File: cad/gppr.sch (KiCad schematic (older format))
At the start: 13 parts

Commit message: create complete schematic
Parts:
- removed C?: C, symbol Device:C
- removed TP?: TestPoint_2Pole, symbol Connector:TestPoint_2Pole
- removed U?: TPS7A470X, Package_DFN_QFN:QFN-20-1EP_5x5mm_P0.65mm_EP3.35x3.35mm, symbol texas_instruments:TPS7A470X
- added C1, C2, C4: 10uF, Capacitor_SMD:C_0805_2012Metric, symbol Device:C
- added C10, C3, C5: 1uF, Capacitor_SMD:C_0805_2012Metric, symbol Device:C
- added C6, C7, C8: 1000uF, Capacitor_SMD:CP_Elec_16x17.5, symbol Device:CP
- added D2, D3, D4: MURS120, Diode_SMD:D_SMB, symbol Device:D
- added H2, H3, H4: MountingHole, MountingHole:MountingHole_3.2mm_M3_DIN965, symbol Mechanical:MountingHole
- added R10: 1KΩ, Resistor_SMD:R_0805_2012Metric, symbol Device:R
- added R2, R3, R4, R5, R6, R7, R8, R9: 0Ω, Resistor_SMD:R_0805_2012Metric_Pad1.15x1.40mm_HandSolder, symbol Device:R
- added TP1, TP2, TP3: TestPoint_2Pole, Connector_pin_header:PinHeader_1x02_P2.54mm_Vertical, symbol Connector:TestPoint_2Pole
- added U1: TPS7A470X, Housings_DFN_QFN:Texas_VQFN-RGW-20, symbol texas_instruments:TPS7A470X
- C9: renamed from C?; value CP -> 1000uF; footprint (none) -> Capacitor_SMD:CP_Elec_16x17.5
- D1: renamed from D?; value D -> MURS120; footprint (none) -> Diode_SMD:D_SMB
- D5: renamed from D?; value D_Zener -> 1SMB5927BT3G; footprint (none) -> Diode_SMD:D_SMB
- D6: renamed from D?; value LED -> LED_POWER; footprint (none) -> LED_SMD:LED_0805_2012Metric
- H1: renamed from H?; footprint (none) -> MountingHole:MountingHole_3.2mm_M3_DIN965
- J3: renamed from J?; footprint (none) -> Connector_Coaxial:U.FL_Molex_MCRF_73412-0110_Vertical
- Q1: renamed from Q?; value QM6006D -> IRLR2908
- R1: renamed from R?; value R -> 13KΩ; footprint (none) -> Resistor_SMD:R_0805_2012Metric
- gave numbers to parts that had none: 2
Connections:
- net at Q1.1 (G): now also D5.1 (K), R1.1, C1.1
- net at Q1.2 (D): now also C9.1, D1.1 (K), R1.2, C6.1, C7.1, C8.1, D3.1 (K), TP1.1
- net at Q1.3 (S): now also D5.2 (A), C2.1, C3.1, TP2.1, U1.13 (EN), U1.15 (IN), U1.16 (IN)
- net at D1.2 (A): now also J1.2 (Pin_2), J1.4 (Pin_4), D2.1 (K)
- net GND: now reaches C9.2
- net GND: now also D6.1 (K), J2.2 (Pin_2), J3.2 (Ext), C1.2, C10.2, C2.2, C3.2, C4.2, C5.2, C6.2, C7.2, C8.2, D2.2 (A), D4.2 (A), R2.2, R3.2, R4.2, R5.2, R6.2, R7.2, R8.2, R9.2, TP1.2, TP2.2, TP3.2, U1.21 (PAD), U1.7 (GND)
- net at D6.2 (A): now also R10.1
- net at J1.1 (Pin_1): now also J1.3 (Pin_3), D3.2 (A), D4.1 (K)
- net at J2.1 (Pin_1): now also J3.1 (In), C4.1, C5.1, R10.2, TP3.1, U1.1 (OUT), U1.20 (OUT), U1.3 (SENSE/FB)
- new net: R4.1, U1.10 (0P4V)
- new net: R3.1, U1.11 (0P2V)
- new net: R2.1, U1.12 (0P1V)
- new net: C10.1, U1.14 (NR)
- new net: R9.1, U1.4 (6P4V2)
- new net: R8.1, U1.5 (6P4V1)
- new net: R7.1, U1.6 (3P2V)
- new net: R6.1, U1.8 (1P6V)
- new net: R5.1, U1.9 (0P8V)
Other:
- moved on the sheet: C9, D1, D5, D6, H1, J1, J2, J3, Q1, R1

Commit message: update schematic: remove any-out, use resistor-divider fb on regulator instead
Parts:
- removed R4, R5, R6, R7, R8, R9: 0Ω, Resistor_SMD:R_0805_2012Metric_Pad1.15x1.40mm_HandSolder, symbol Device:R
- R1: renamed from R2; value 0Ω -> 76.8KΩ
- R2: renamed from R3; value 0Ω -> 10.2KΩ
- renumbered R10 to R3, R1 to R4
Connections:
- net GND: now also R2.1; no longer R1.2, R2.2
- net at C4.1, C5.1, J2.1 (Pin_1)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: now also R1.2; no longer U1.3 (SENSE/FB)
- net at U1.11 (0P2V): no longer R2.1
- net at U1.12 (0P1V): no longer R1.1
- new net: R1.1, R2.2, U1.3 (SENSE/FB)
- no-connect marks 0 -> 8
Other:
- moved on the sheet: C4, C5, R1, R2

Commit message: add missing footprint references for in/out connectors
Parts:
- J1: footprint (none) -> Connector_Molex:Molex_Mini-Fit_Jr_5566-04A_2x02_P4.20mm_Vertical
- J2: footprint (none) -> Connector_Molex:Molex_Mini-Fit_Jr_5566-02A_2x01_P4.20mm_Vertical
- Q1: footprint Package_TO_SOT_SMD:TO-252-2 -> TO_SOT_Packages_SMD:TO-252-2
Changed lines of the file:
@@
 F 0 "Q1" H 4805 4146 50  0000 L CNN
 F 1 "IRLR2908" H 4805 4055 50  0000 L CNN
-F 2 "Package_TO_SOT_SMD:TO-252-2" H 4800 4025 50  0001 L CIN
+F 2 "TO_SOT_Packages_SMD:TO-252-2" H 4800 4025 50  0001 L CIN
 F 3 "https://www.infineon.com/dgdl/irlr2908pbf.pdf?fileId=5546d462533600a40153566cdace2681" H 4400 4400 50  0001 L CNN
 	1    4600 4100
@@
 F 0 "J1" H 600 5000 50  0000 L CNN
 F 1 "Conn_01x04_Female" H -50 5100 50  0000 L CNN
-F 2 "" H 750 4500 50  0001 C CNN
+F 2 "Connector_Molex:Molex_Mini-Fit_Jr_5566-04A_2x02_P4.20mm_Vertical" H 750 4500 50  0001 C CNN
 F 3 "~" H 750 4500 50  0001 C CNN
 	1    750  4500
@@
 F 0 "J2" H 10650 4300 50  0000 L CNN
 F 1 "Conn_01x02_Female" H 10150 4200 50  0000 L CNN
-F 2 "" H 10900 4000 50  0001 C CNN
+F 2 "Connector_Molex:Molex_Mini-Fit_Jr_5566-02A_2x01_P4.20mm_Vertical" H 10900 4000 50  0001 C CNN
 F 3 "~" H 10900 4000 50  0001 C CNN
 	1    10900 4000

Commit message: add simple calcs for max input voltage for safe operation
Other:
- note added: "Capacitors: Panasonic EEV-FK1H102M"
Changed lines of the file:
@@
 	7050 4550 7050 4000
 Connection ~ 7050 4000
+Text Notes 2300 3850 0    50   ~ 0
+Capacitors: Panasonic EEV-FK1H102M
 $EndSCHEMATC

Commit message: generate netlist
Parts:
- J1: footprint Connector_Molex:Molex_Mini-Fit_Jr_5566-04A_2x02_P4.20mm_Vertical -> Connector_Molex:Molex_Micro-Fit_3.0_43045-0412_2x02_P3.00mm_Vertical
- J2: footprint Connector_Molex:Molex_Mini-Fit_Jr_5566-02A_2x01_P4.20mm_Vertical -> Connector_Molex:Molex_Micro-Fit_3.0_43045-0212_2x01_P3.00mm_Vertical
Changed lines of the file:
@@
 F 0 "J1" H 600 5000 50  0000 L CNN
 F 1 "Conn_01x04_Female" H -50 5100 50  0000 L CNN
-F 2 "Connector_Molex:Molex_Mini-Fit_Jr_5566-04A_2x02_P4.20mm_Vertical" H 750 4500 50  0001 C CNN
+F 2 "Connector_Molex:Molex_Micro-Fit_3.0_43045-0412_2x02_P3.00mm_Vertical" H 750 4500 50  0001 C CNN
 F 3 "~" H 750 4500 50  0001 C CNN
 	1    750  4500
@@
 F 0 "J2" H 10650 4300 50  0000 L CNN
 F 1 "Conn_01x02_Female" H 10150 4200 50  0000 L CNN
-F 2 "Connector_Molex:Molex_Mini-Fit_Jr_5566-02A_2x01_P4.20mm_Vertical" H 10900 4000 50  0001 C CNN
+F 2 "Connector_Molex:Molex_Micro-Fit_3.0_43045-0212_2x01_P3.00mm_Vertical" H 10900 4000 50  0001 C CNN
 F 3 "~" H 10900 4000 50  0001 C CNN
 	1    10900 4000

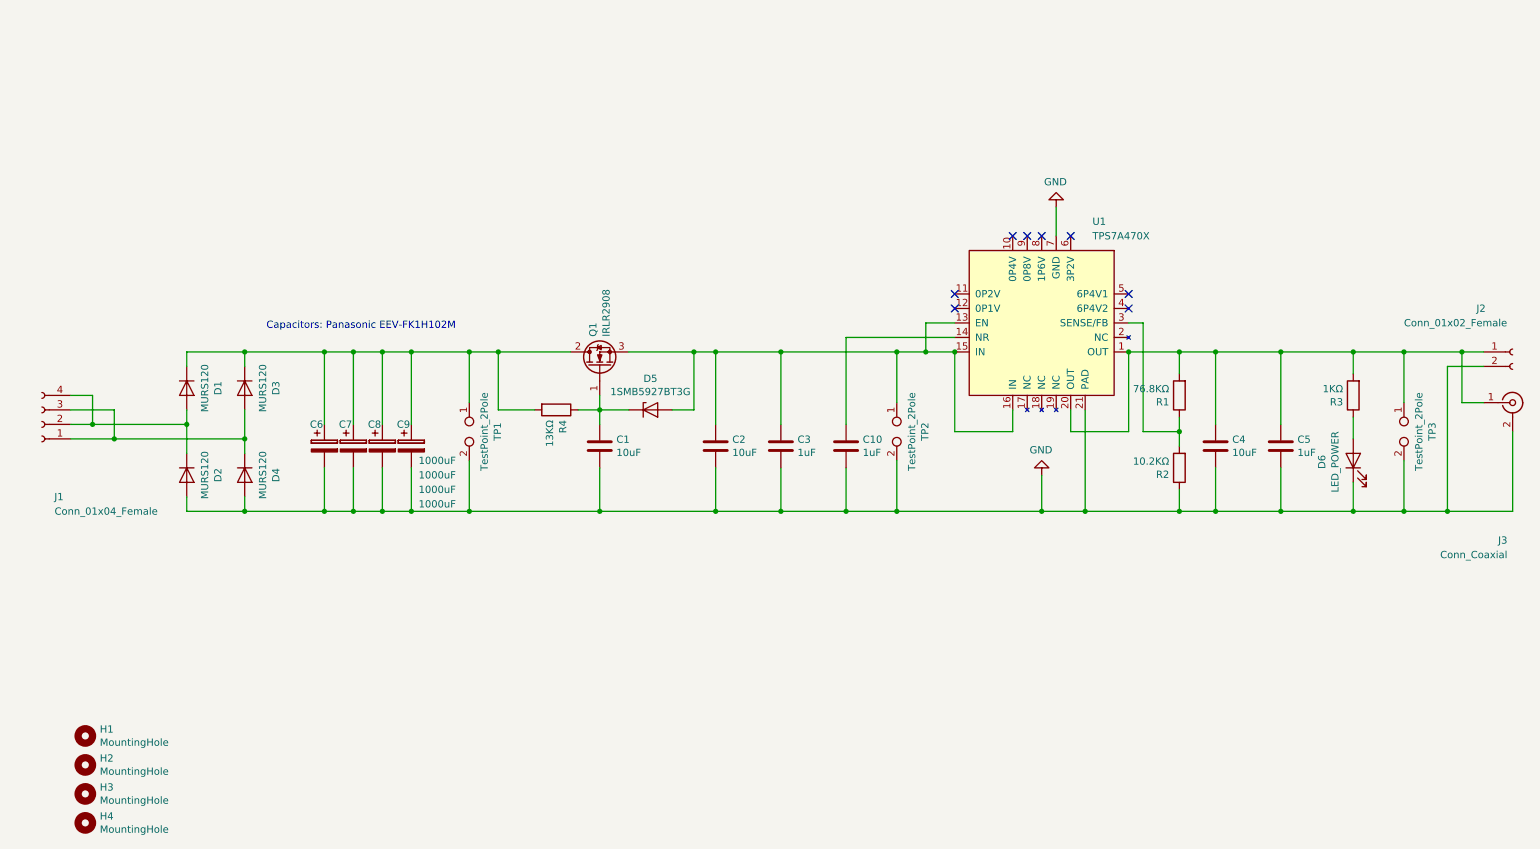
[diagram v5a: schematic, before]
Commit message: add jumper-resistors, change ceramic film capacitor packages
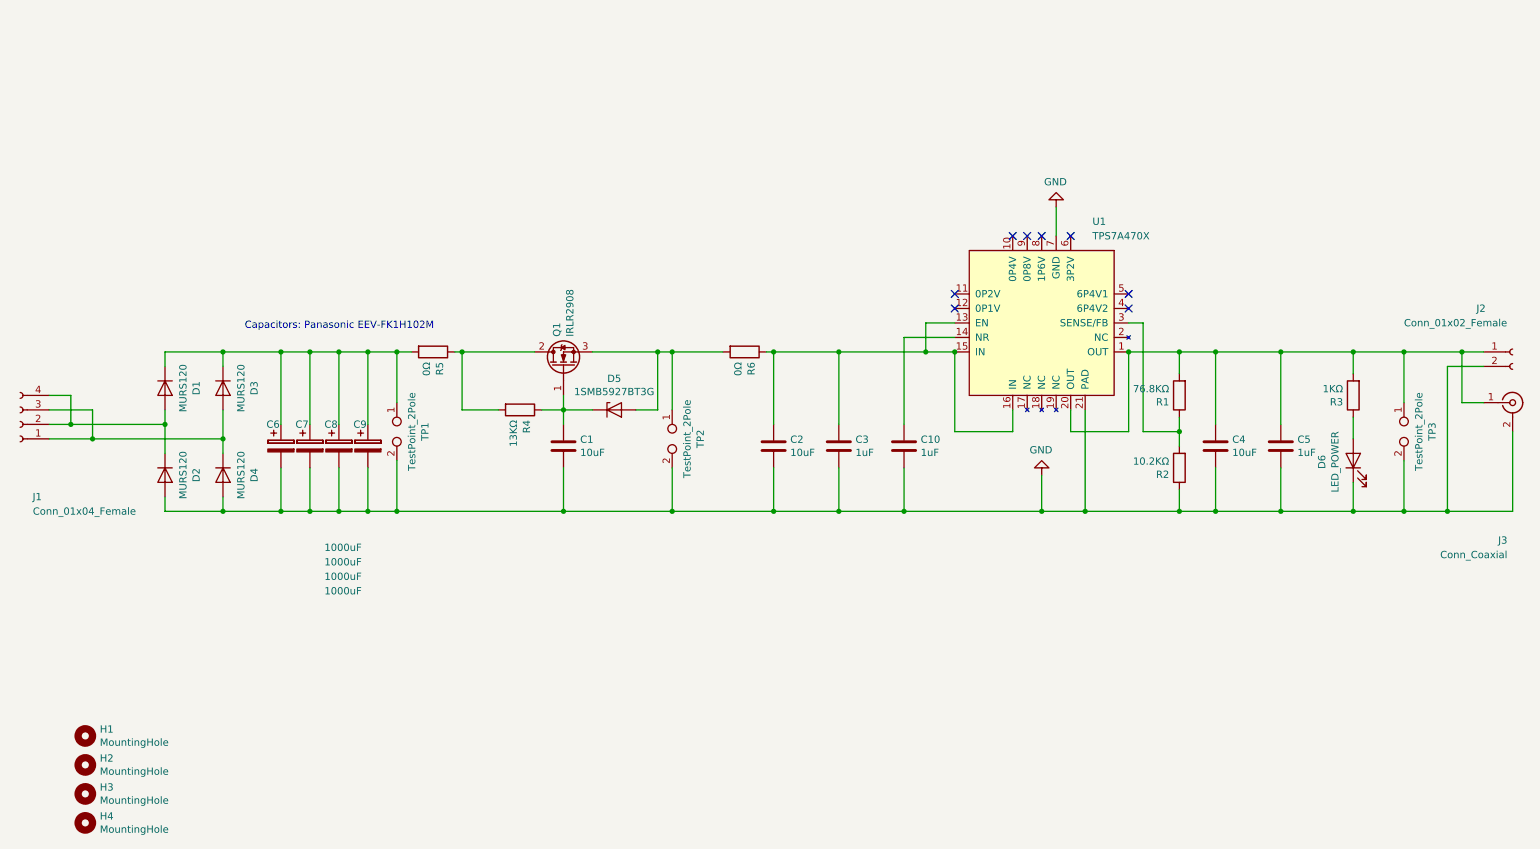
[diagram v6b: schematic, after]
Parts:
- added R5, R6: 0Ω, Resistor_SMD:R_0805_2012Metric, symbol Device:R
- C1, C2, C4: footprint Capacitor_SMD:C_0805_2012Metric -> Capacitor_SMD:C_1210_3225Metric
- C10, C3, C5: footprint Capacitor_SMD:C_0805_2012Metric -> Capacitor_SMD:C_1206_3216Metric
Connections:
- net at C6.1, C7.1, C8.1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: now also R5.2; no longer Q1.2 (D), R4.2
- net at C2.1, C3.1, U1.13 (EN)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: now also R6.1; no longer D5.2 (A), Q1.3 (S), TP2.1
- new net: Q1.2 (D), R4.2, R5.1
- new net: D5.2 (A), Q1.3 (S), R6.2, TP2.1
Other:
- moved on the sheet: C1, C10, C2, C3, C6, C7, C8, C9, D1, D2, D3, D4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

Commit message: basic component placement, prep for trace routing
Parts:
- added HS1: Heatsink_Pad, Heatsink:Heatsink_960-23-XX-F-AB-0, symbol Mechanical:Heatsink_Pad
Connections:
- wire segments 119 -> 120
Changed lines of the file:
@@
 L power:GND #PWR0103
 U 1 1 5D2B8477
-P 7650 4850
-F 0 "#PWR0103" H 7650 4600 50  0001 C CNN
-F 1 "GND" H 7655 4677 50  0000 C CNN
-F 2 "" H 7650 4850 50  0001 C CNN
-F 3 "" H 7650 4850 50  0001 C CNN
-	1    7650 4850
-	-1   0    0    1
-$EndComp
-Wire Wire Line
-	7650 4850 7650 5100
+P 8000 4900
+F 0 "#PWR0103" H 8000 4650 50  0001 C CNN
+F 1 "GND" H 8005 4727 50  0000 C CNN
+F 2 "" H 8000 4900 50  0001 C CNN
+F 3 "" H 8000 4900 50  0001 C CNN
+	1    8000 4900
+	0    -1   -1   0
+$EndComp
 Wire Wire Line
 	800  4600 1100 4600
@@
 $EndComp
 Wire Wire Line
-	7950 4400 7950 5100
-Wire Wire Line
-	7950 5100 7650 5100
+	7950 4400 7950 4900
 $Comp
 L texas_instruments:TPS7A470X U1
@@
 Connection ~ 6250 4000
 Connection ~ 6850 4000
-Wire Wire Line
-	6700 5100 7650 5100
 Connection ~ 6700 5100
-Connection ~ 7650 5100
 Connection ~ 5800 5100
 $Comp
@@
 Connection ~ 2400 5100
 Connection ~ 2000 5100
+$Comp
+L Mechanical:Heatsink_Pad HS1
+U 1 1 5D29E9DA
+P 7650 4900
+F 0 "HS1" V 7929 4895 50  0000 C CNN
+F 1 "Heatsink_Pad" V 7838 4895 50  0000 C CNN
+F 2 "Heatsink:Heatsink_960-23-XX-F-AB-0" H 7662 4850 50  0001 C CNN
+F 3 "~" H 7662 4850 50  0001 C CNN
+	1    7650 4900
+	0    -1   -1   0
+$EndComp
+Wire Wire Line
+	6700 5100 7950 5100
+Wire Wire Line
+	7750 4900 7950 4900
+Connection ~ 7950 4900
+Wire Wire Line
+	7950 4900 7950 5100
+Wire Wire Line
+	7950 4900 8000 4900
 $EndSCHEMATC

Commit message: change heatsink footprint from bottom to top side
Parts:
- HS1: footprint Heatsink:Heatsink_960-23-XX-F-AB-0 -> Heatsink:Heatsink_960-23-XX-F-AB-0_Top
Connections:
- wire segments 120 -> 125
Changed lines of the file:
@@
 L power:GND #PWR0103
 U 1 1 5D2B8477
-P 8000 4900
-F 0 "#PWR0103" H 8000 4650 50  0001 C CNN
-F 1 "GND" H 8005 4727 50  0000 C CNN
-F 2 "" H 8000 4900 50  0001 C CNN
-F 3 "" H 8000 4900 50  0001 C CNN
-	1    8000 4900
-	0    -1   -1   0
+P 7950 5350
+F 0 "#PWR0103" H 7950 5100 50  0001 C CNN
+F 1 "GND" H 7955 5177 50  0000 C CNN
+F 2 "" H 7950 5350 50  0001 C CNN
+F 3 "" H 7950 5350 50  0001 C CNN
+	1    7950 5350
+	1    0    0    -1
 $EndComp
 Wire Wire Line
@@
 	0    1    1    0
 $EndComp
-Wire Wire Line
-	7950 4400 7950 4900
-$Comp
-L texas_instruments:TPS7A470X U1
-U 1 1 5D235CDE
-P 8150 3300
-F 0 "U1" H 8300 3100 50  0000 R CNN
-F 1 "TPS7A470X" H 8300 3200 50  0000 R CNN
-F 2 "Housings_DFN_QFN:Texas_VQFN-RGW-20" H 8650 2800 50  0001 C CNN
-F 3 "http://www.ti.com/lit/ds/symlink/tps7a47.pdf" H 8650 2800 50  0001 C CNN
-	1    8150 3300
-	-1   0    0    1
-$EndComp
 NoConn ~ 7050 3700
 NoConn ~ 7050 3600
@@
 Wire Wire Line
 	7850 4550 7850 4400
-Connection ~ 8250 4000
 Wire Wire Line
 	7450 4400 7450 4550
@@
 Wire Wire Line
 	7050 4550 7050 4000
-Connection ~ 7050 4000
 Text Notes 2150 3850 0    50   ~ 0
 Capacitors: Panasonic EEV-FK1H102M
@@
 L Mechanical:Heatsink_Pad HS1
 U 1 1 5D29E9DA
-P 7650 4900
-F 0 "HS1" V 7929 4895 50  0000 C CNN
-F 1 "Heatsink_Pad" V 7838 4895 50  0000 C CNN
-F 2 "Heatsink:Heatsink_960-23-XX-F-AB-0" H 7662 4850 50  0001 C CNN
-F 3 "~" H 7662 4850 50  0001 C CNN
-	1    7650 4900
-	0    -1   -1   0
-$EndComp
-Wire Wire Line
-	6700 5100 7950 5100
-Wire Wire Line
-	7750 4900 7950 4900
-Connection ~ 7950 4900
-Wire Wire Line
-	7950 4900 7950 5100
-Wire Wire Line
-	7950 4900 8000 4900
+P 7550 5450
+F 0 "HS1" V 7829 5445 50  0000 C CNN
+F 1 "Heatsink_Pad" V 7738 5445 50  0000 C CNN
+F 2 "Heatsink:Heatsink_960-23-XX-F-AB-0_Top" H 7562 5400 50  0001 C CNN
+F 3 "~" H 7562 5400 50  0001 C CNN
+	1    7550 5450
+	-1   0    0    1
+$EndComp
+Wire Wire Line
+	6700 5100 7550 5100
+$Comp
+L texas_instruments:TPS7A470X U1
+U 1 1 5D353278
+P 8150 3300
+F 0 "U1" H 8009 3754 50  0000 R CNN
+F 1 "TPS7A470X" H 8009 3845 50  0000 R CNN
+F 2 "Housings_DFN_QFN:Texas_VQFN-RGW-20" H 8650 2800 50  0001 C CNN
+F 3 "http://www.ti.com/lit/ds/symlink/tps7a47.pdf" H 8650 2800 50  0001 C CNN
+	1    8150 3300
+	-1   0    0    1
+$EndComp
+Connection ~ 8250 4000
+Connection ~ 7050 4000
+Wire Wire Line
+	7950 4400 7950 5100
+Wire Wire Line
+	7950 5100 7950 5350
+Wire Wire Line
+	7750 4400 7750 5100
+Connection ~ 7750 5100
+Wire Wire Line
+	7750 5100 7950 5100
+Wire Wire Line
+	7550 4400 7550 5100
+Connection ~ 7550 5100
+Wire Wire Line
+	7550 5100 7650 5100
+Wire Wire Line
+	7550 5100 7550 5350
+Wire Wire Line
+	7650 4400 7650 5100
+Connection ~ 7650 5100
+Wire Wire Line
+	7650 5100 7750 5100
 $EndSCHEMATC
